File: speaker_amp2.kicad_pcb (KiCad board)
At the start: 2 copper layers, 74 parts, among them J1 Molex_430450227, J2 Molex_430450227, J3 Molex_430450227, J4 Molex_430450227, J5 Molex_1053101106, J6 Molex_430450227, U1 TAS5822MDCPR, U2 TAS5822MDCPR

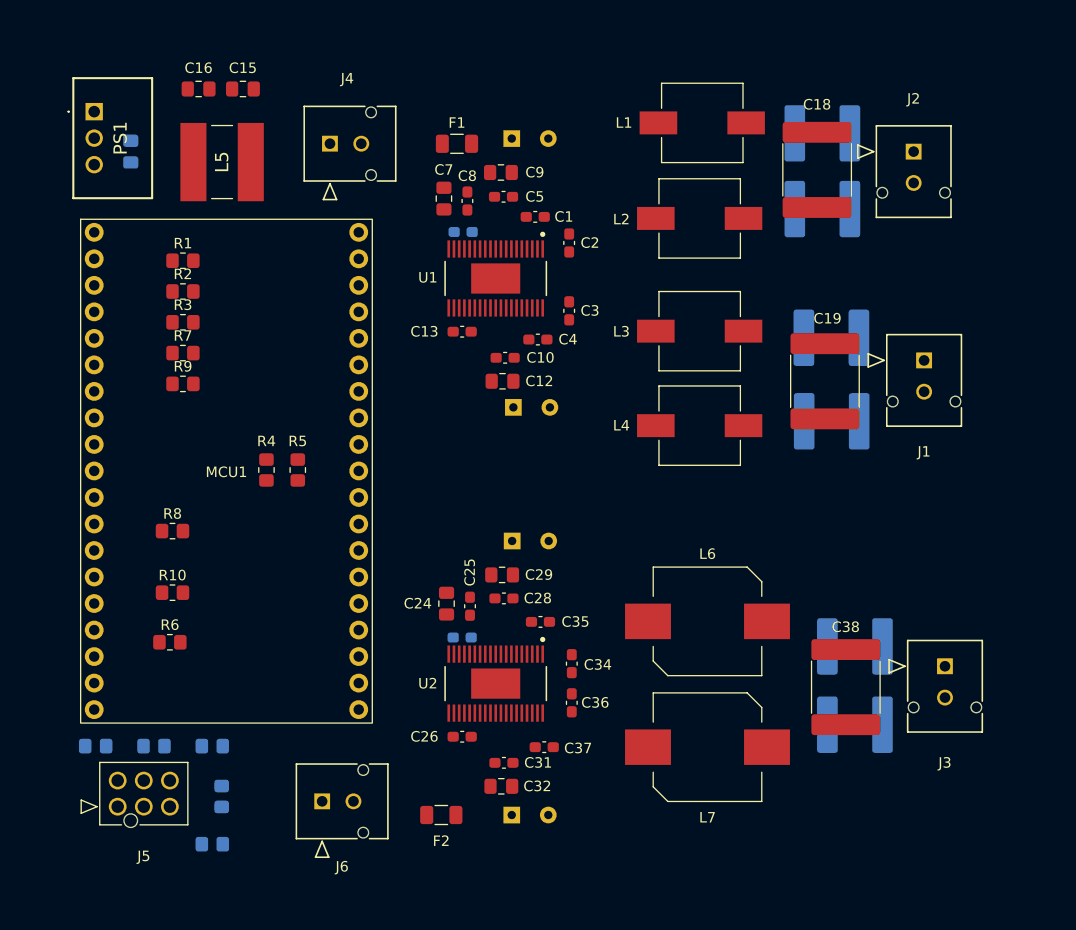
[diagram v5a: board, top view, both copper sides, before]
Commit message: finalized pcb component placement; started connections
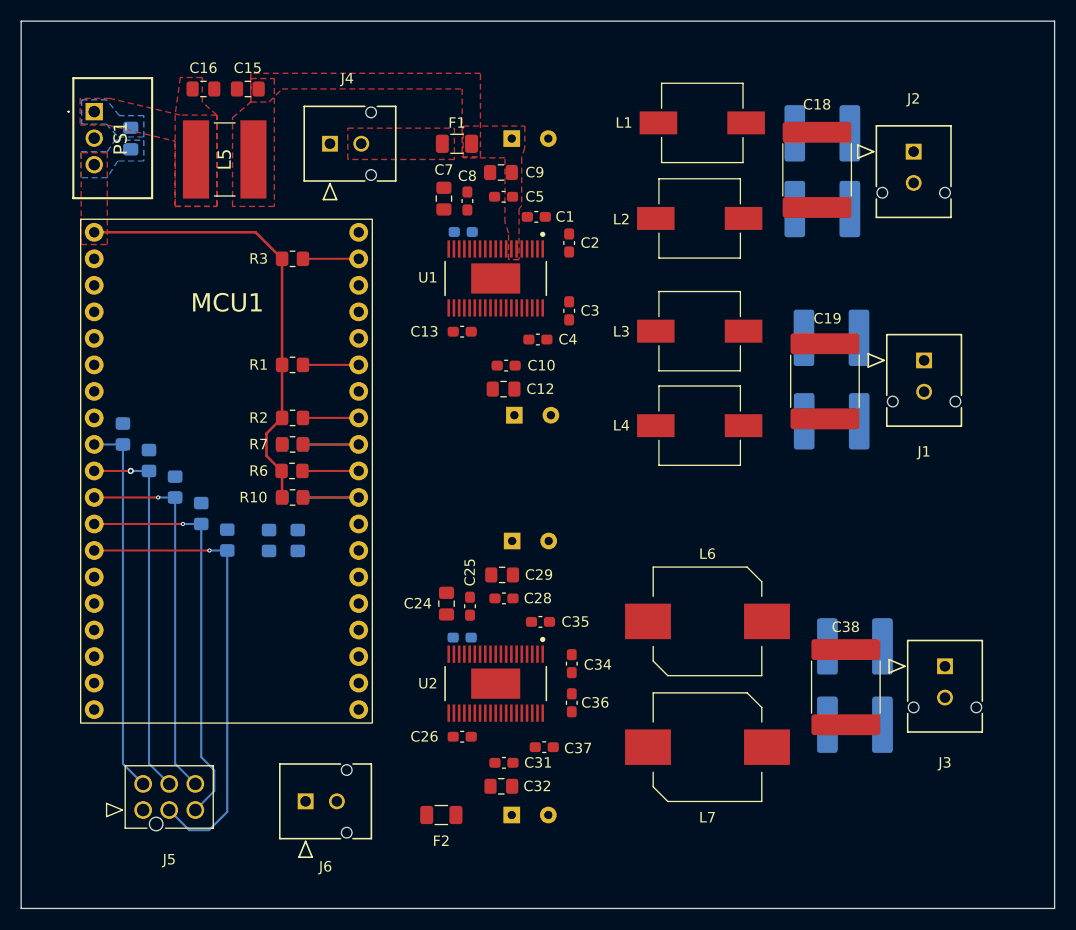
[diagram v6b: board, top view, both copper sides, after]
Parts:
- R4, R5, R8, R9: moved to B.Cu
- moved R13 30.0 mm to (49.0, 104.5), turned to 90 degrees
- moved R11 29.2 mm to (59.0, 114.7), turned to 90 degrees
- moved R14 27.4 mm to (51.5, 107.1), turned to 90 degrees
- moved R12 27.2 mm to (56.5, 112.2)
- moved R15 25.1 mm to (54.0, 109.6), turned to 90 degrees
- moved R6 20.2 mm to (65.2, 108.1), turned to 180 degrees
- moved R2 16.0 mm to (65.2, 103.0), turned to 180 degrees
- moved R10 14.7 mm to (65.2, 110.6), turned to 180 degrees
- moved R1 14.5 mm to (65.2, 97.9), turned to 180 degrees
- moved R7 13.7 mm to (65.2, 105.5), turned to 180 degrees
- moved R3 12.1 mm to (65.2, 87.8), turned to 180 degrees
- moved R9 12.0 mm to (65.2, 105.5), turned to 180 degrees
- moved R8 11.9 mm to (65.2, 110.6), turned to 180 degrees
- moved R4 6.75 mm to (63.0, 114.8)
- moved R5 6.75 mm to (65.8, 114.8)
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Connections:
- MCU1 pad 13: unconnected-(MCU1-GPIO12-Pad13) -> /Previous
- MCU1 pad 8: /Previous -> unconnected-(MCU1-GPIO33-Pad8)
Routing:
- net /Previous: track 0.00 -> 44.9 mm, vias 0 -> 1
- net +3.3V: track 0.00 -> 43.2 mm
- net /Next: track 0.00 -> 39.0 mm, vias 0 -> 1
- net /Volume-: track 0.00 -> 36.1 mm
- net /Volume+: track 0.00 -> 36.0 mm, vias 0 -> 1
- net /Play/Pause: track 0.00 -> 36.0 mm, vias 0 -> 1
- net /PDN2: track 0.00 -> 10.7 mm
- net /PDN1: track 0.00 -> 10.7 mm
- net /ADR2: track 0.00 -> 5.39 mm
- net /SDA: track 0.00 -> 5.34 mm
- net /SCL: track 0.00 -> 5.34 mm
- net /ADR1: track 0.00 -> 5.34 mm
- added copper zone on B.Cu, net +3.3V
- added copper zone on F.Cu, net +3.3V
- added copper zone on F.Cu, net Net-(F1-Pad2)
- added copper zone on B.Cu, net Net-(PS1-+VIN)
- added copper zone on F.Cu, net Net-(PS1-+VIN)
- added copper zone on F.Cu, net PVDD
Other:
- board outline added: 99 x 85 mm

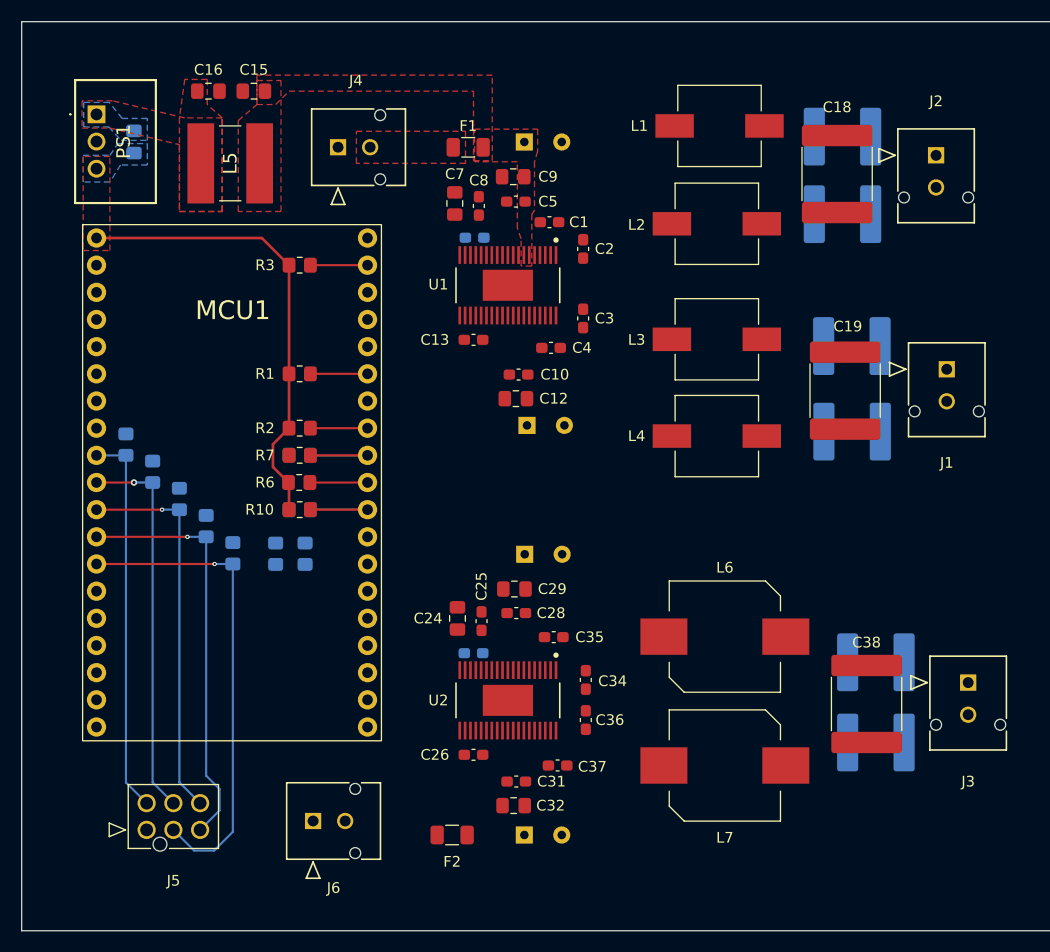
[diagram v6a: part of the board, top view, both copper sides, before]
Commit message: started working on subwoofer amp traces
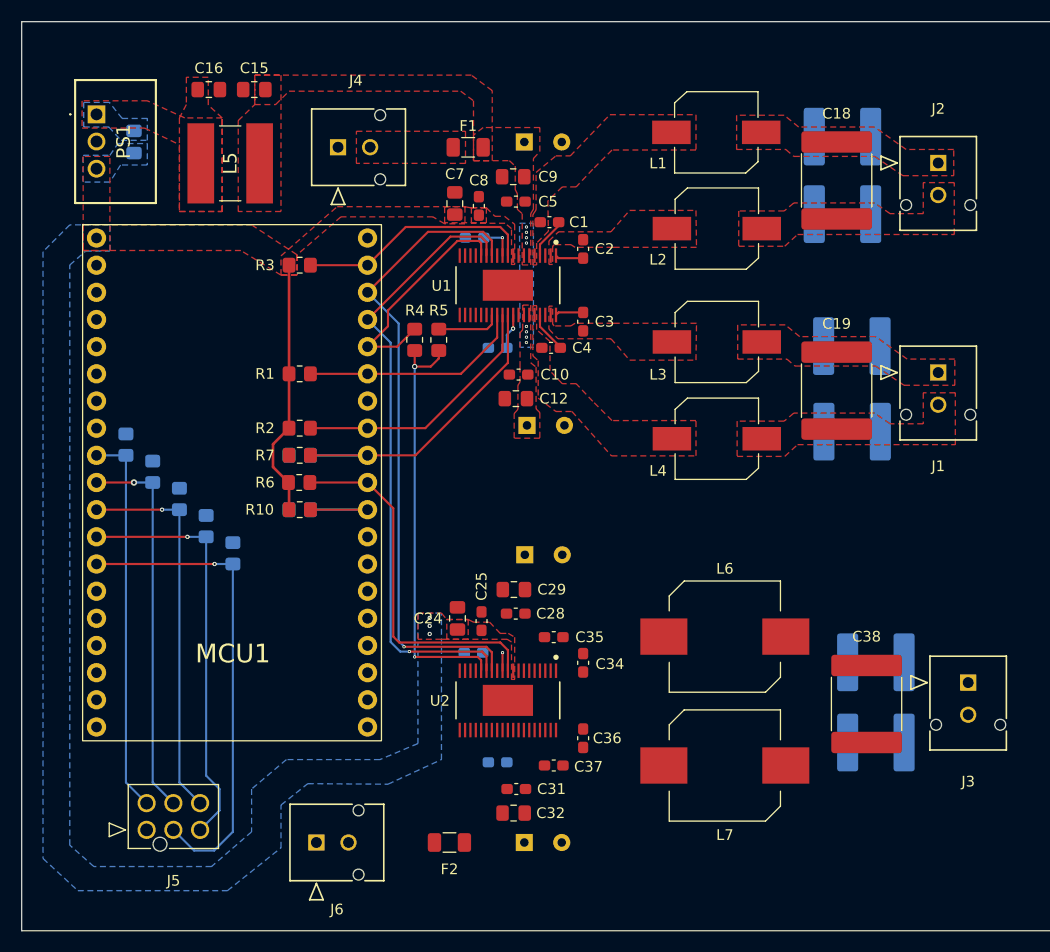
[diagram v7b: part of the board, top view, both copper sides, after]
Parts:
- C13, C26: moved to B.Cu
- L1, L2, L3, L4: footprint Inductor_SMD:L_Wuerth_WE-PD-Typ-M-Typ-S_Handsoldering -> Speaker Amp Lib:WE_7447773220
- R4, R5: moved to F.Cu
- U1, U2: footprint Speaker Amp Lib:DCP0038A-IPC_B -> Speaker Amp Lib:DCP0038A-IPC_C
- moved R4 23.9 mm to (76.0, 94.8)
- moved R5 23.6 mm to (78.2, 94.8)
- moved C13 2.37 mm to (83.8, 95.5)
- moved C26 2.36 mm to (83.8, 134.2)
- moved J6 2.03 mm to (66.8, 141.8)
- moved C36 1.72 mm to (91.8, 132.0)
- moved C34 1.62 mm to (91.8, 125.0)
- moved J1 0.86 mm to (125.0, 97.8)
- moved C19 0.80 mm to (115.5, 99.5)
- moved F2 0.74 mm to (79.2, 141.8)
- moved J2 0.74 mm to (125.0, 78.2)
- moved C31 0.70 mm to (85.5, 136.8)
- moved C32 0.70 mm to (85.2, 139.0)
- moved C33 0.70 mm to (86.2, 141.8)
- moved L1 0.67 mm to (104.2, 75.3)
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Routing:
- net /LRCLK: track 0.00 -> 60.4 mm, vias 0 -> 1
- net /SCLK: track 0.00 -> 57.7 mm, vias 0 -> 1
- net Net-(U2-SDIN): track 0.00 -> 39.3 mm, vias 0 -> 2
- net /ADR2: track 5.39 -> 34.0 mm
- net /SDIN: track 0.00 -> 21.9 mm
- net /PDN1: track 10.7 -> 31.9 mm
- net +3.3V: track 43.2 -> 24.1 mm, vias 0 -> 3
- net /SCL: track 5.34 -> 24.3 mm
- net /ADR1: track 5.34 -> 22.2 mm
- net /SDA: track 5.34 -> 21.0 mm
- net /SDOUT1: track 0.00 -> 6.03 mm
- net Net-(U1-BST_B+): track 0.00 -> 3.86 mm
- net Net-(U1-BST_A+): track 0.00 -> 3.85 mm
- net Net-(U1-VR_DIG): track 0.00 -> 3.42 mm, vias 0 -> 1
- net Net-(U1-AVDD): track 0.00 -> 3.32 mm, vias 0 -> 1
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- added copper zone on F.Cu, net Net-(C18-Pad1)
- added copper zone on F.Cu, net Net-(C18-Pad2)
- added copper zone on F.Cu, net Net-(C19-Pad1)
- added copper zone on F.Cu, net Net-(C19-Pad2)
- added copper zone on F.Cu, net Net-(U1-OUT_A+)
- added copper zone on F.Cu, net Net-(U1-OUT_A-)
- added copper zone on F.Cu, net Net-(U1-OUT_B+)
- added copper zone on F.Cu, net Net-(U1-OUT_B-)
- added copper zone on B.Cu, net PVDD

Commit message: first finalized pcb
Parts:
- moved C23 0.98 mm to (116.0, 102.8)
- moved C21 0.83 mm to (116.0, 95.5)
- moved C39 0.66 mm to (118.8, 131.8)
- moved C40 0.51 mm to (118.8, 124.5)
- moved C4 0.50 mm to (88.8, 96.0)
- moved C1 0.40 mm to (88.6, 83.3)
- moved C35 0.35 mm to (89.0, 122.2), turned to 180 degrees
- moved C20 0.25 mm to (116.0, 83.2)
- moved C22 0.25 mm to (116.0, 76.0)
- moved C38 0.25 mm to (118.2, 128.6)
- moved C37 0.20 mm to (89.0, 134.8), turned to 0 degrees
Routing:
- net /SDA: track 21.0 -> 77.3 mm, vias 0 -> 1
- net /SCL: track 24.3 -> 77.2 mm, vias 0 -> 1
- net /PDN2: track 10.7 -> 45.4 mm
- net Net-(U2-BST_B+): track 0.00 -> 4.40 mm
- net Net-(U2-BST_A+): track 0.00 -> 4.38 mm
- net Net-(U2-AVDD): track 0.00 -> 3.26 mm, vias 0 -> 1
- net Net-(U2-BST_A-): track 0.00 -> 2.59 mm
- net Net-(U2-BST_B-): track 0.00 -> 2.58 mm
- net Net-(U2-VR_DIG): track 1.69 -> 3.54 mm
- net /PDN1: track 31.9 -> 31.2 mm
- net PVDD2: vias 0 -> 8
- net GND: vias 0 -> 2
- added copper zone on B.Cu, net GND
- added copper zone on F.Cu, net GND
- added copper zone on B.Cu, net Net-(C18-Pad1)
- added copper zone on B.Cu, net Net-(C18-Pad2)
- added copper zone on B.Cu, net Net-(C19-Pad1)
- added copper zone on B.Cu, net Net-(C19-Pad2)
- added copper zone on B.Cu, net Net-(C38-Pad1)
- added copper zone on F.Cu, net Net-(C38-Pad1)
- added copper zone on B.Cu, net Net-(C38-Pad2)
- added copper zone on F.Cu, net Net-(C38-Pad2)
- added copper zone on F.Cu, net Net-(F2-Pad2)
- added copper zone on F.Cu, net Net-(U2-OUT_A+)
- added copper zone on F.Cu, net Net-(U2-OUT_B+)
- added copper zone on B.Cu, net PVDD2
- added copper zone on F.Cu, net PVDD2
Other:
- board size 99 x 85 mm -> 100 x 85 mm
